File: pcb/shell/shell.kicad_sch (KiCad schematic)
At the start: 206 parts, among them J1 Conn_01x11, J2 Conn_01x11

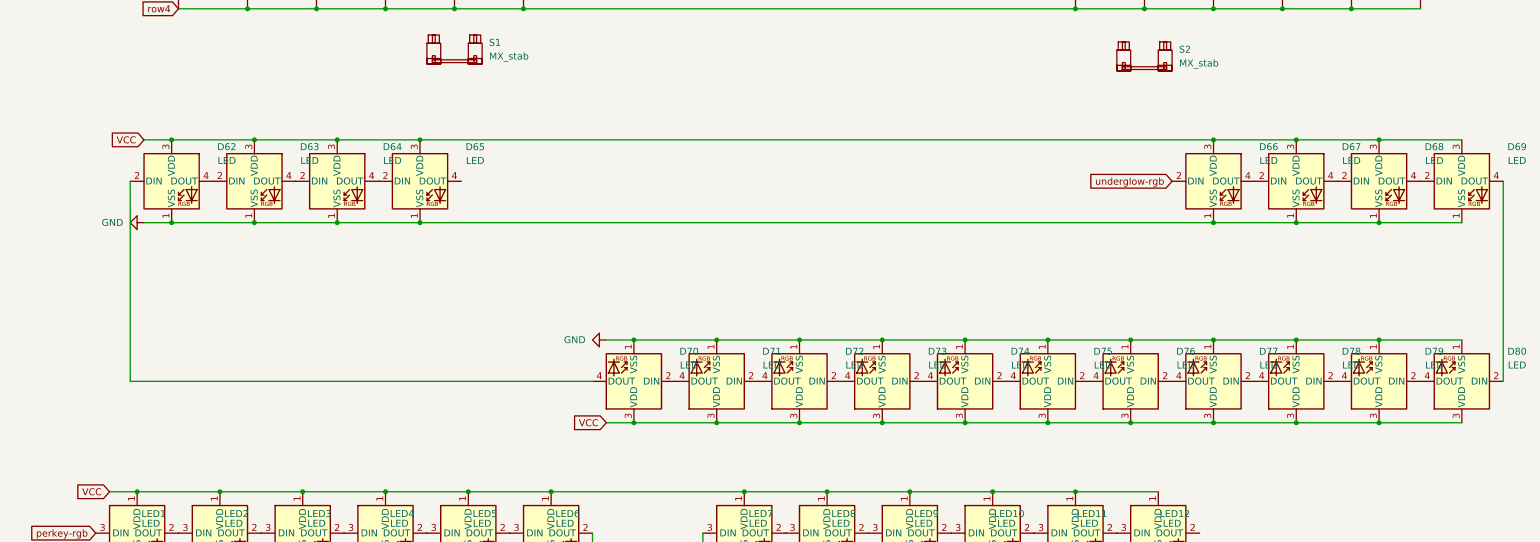
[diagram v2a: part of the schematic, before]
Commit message: added underglow rgb
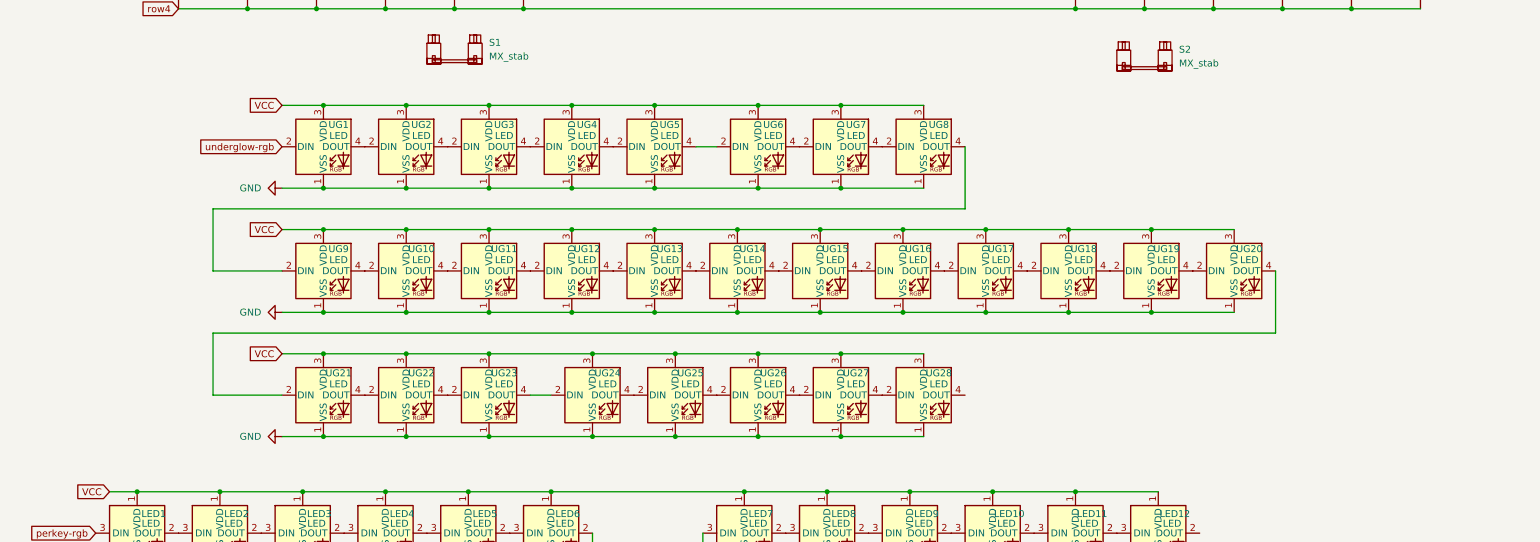
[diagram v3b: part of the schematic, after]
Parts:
- removed D62, D63, D64, D65, D67, D68, D69, D70, D71, D72, D73, D74, D75, D76, D77, D78, D79, D80: LED, LED_SMD:LED_SK6812_PLCC4_5.0x5.0mm_P3.2mm, symbol LED:SK6812
- added UG10, UG11, UG12, UG13, UG14, UG15, UG16, UG17, UG18, UG19, UG2, UG20, UG21, UG22, UG23, UG24, UG25, UG26, UG27, UG28, UG3, UG4, UG5, UG6, UG7, UG8, UG9: LED, LED_SMD:LED_SK6812_PLCC4_5.0x5.0mm_P3.2mm, symbol LED:SK6812
- renumbered D66 to UG1
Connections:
- net GND: now also UG10.1 (VSS), UG11.1 (VSS), UG12.1 (VSS), UG13.1 (VSS), UG14.1 (VSS), UG15.1 (VSS), UG16.1 (VSS), UG17.1 (VSS), UG18.1 (VSS), UG19.1 (VSS), UG2.1 (VSS), UG20.1 (VSS), UG21.1 (VSS), UG22.1 (VSS), UG23.1 (VSS), UG24.1 (VSS), UG25.1 (VSS), UG26.1 (VSS), UG27.1 (VSS), UG28.1 (VSS), UG3.1 (VSS), UG4.1 (VSS), UG5.1 (VSS), UG6.1 (VSS), UG7.1 (VSS), UG8.1 (VSS), UG9.1 (VSS)
- net VCC: now also UG10.3 (VDD), UG11.3 (VDD), UG12.3 (VDD), UG13.3 (VDD), UG14.3 (VDD), UG15.3 (VDD), UG16.3 (VDD), UG17.3 (VDD), UG18.3 (VDD), UG19.3 (VDD), UG2.3 (VDD), UG20.3 (VDD), UG21.3 (VDD), UG22.3 (VDD), UG23.3 (VDD), UG24.3 (VDD), UG25.3 (VDD), UG26.3 (VDD), UG27.3 (VDD), UG28.3 (VDD), UG3.3 (VDD), UG4.3 (VDD), UG5.3 (VDD), UG6.3 (VDD), UG7.3 (VDD), UG8.3 (VDD), UG9.3 (VDD)
- net at UG1.4 (DOUT): now also UG2.2 (DIN)
- new net: UG16.4 (DOUT), UG17.2 (DIN)
- new net: UG17.4 (DOUT), UG18.2 (DIN)
- new net: UG10.4 (DOUT), UG11.2 (DIN)
- new net: UG11.4 (DOUT), UG12.2 (DIN)
- new net: UG13.4 (DOUT), UG14.2 (DIN)
- new net: UG14.4 (DOUT), UG15.2 (DIN)
- new net: UG15.4 (DOUT), UG16.2 (DIN)
- new net: UG26.4 (DOUT), UG27.2 (DIN)
- new net: UG27.4 (DOUT), UG28.2 (DIN)
- new net: UG19.4 (DOUT), UG20.2 (DIN)
- new net: UG20.4 (DOUT), UG21.2 (DIN)
- new net: UG18.4 (DOUT), UG19.2 (DIN)
- new net: UG8.4 (DOUT), UG9.2 (DIN)
- new net: UG10.2 (DIN), UG9.4 (DOUT)
- new net: UG22.4 (DOUT), UG23.2 (DIN)
- new net: UG23.4 (DOUT), UG24.2 (DIN)
- new net: UG21.4 (DOUT), UG22.2 (DIN)
- new net: UG6.4 (DOUT), UG7.2 (DIN)
- new net: UG7.4 (DOUT), UG8.2 (DIN)
- new net: UG24.4 (DOUT), UG25.2 (DIN)
- new net: UG25.4 (DOUT), UG26.2 (DIN)
- new net: UG2.4 (DOUT), UG3.2 (DIN)
- new net: UG3.4 (DOUT), UG4.2 (DIN)
- new net: UG12.4 (DOUT), UG13.2 (DIN)
- new net: UG4.4 (DOUT), UG5.2 (DIN)
- new net: UG5.4 (DOUT), UG6.2 (DIN)
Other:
- moved on the sheet: UG1

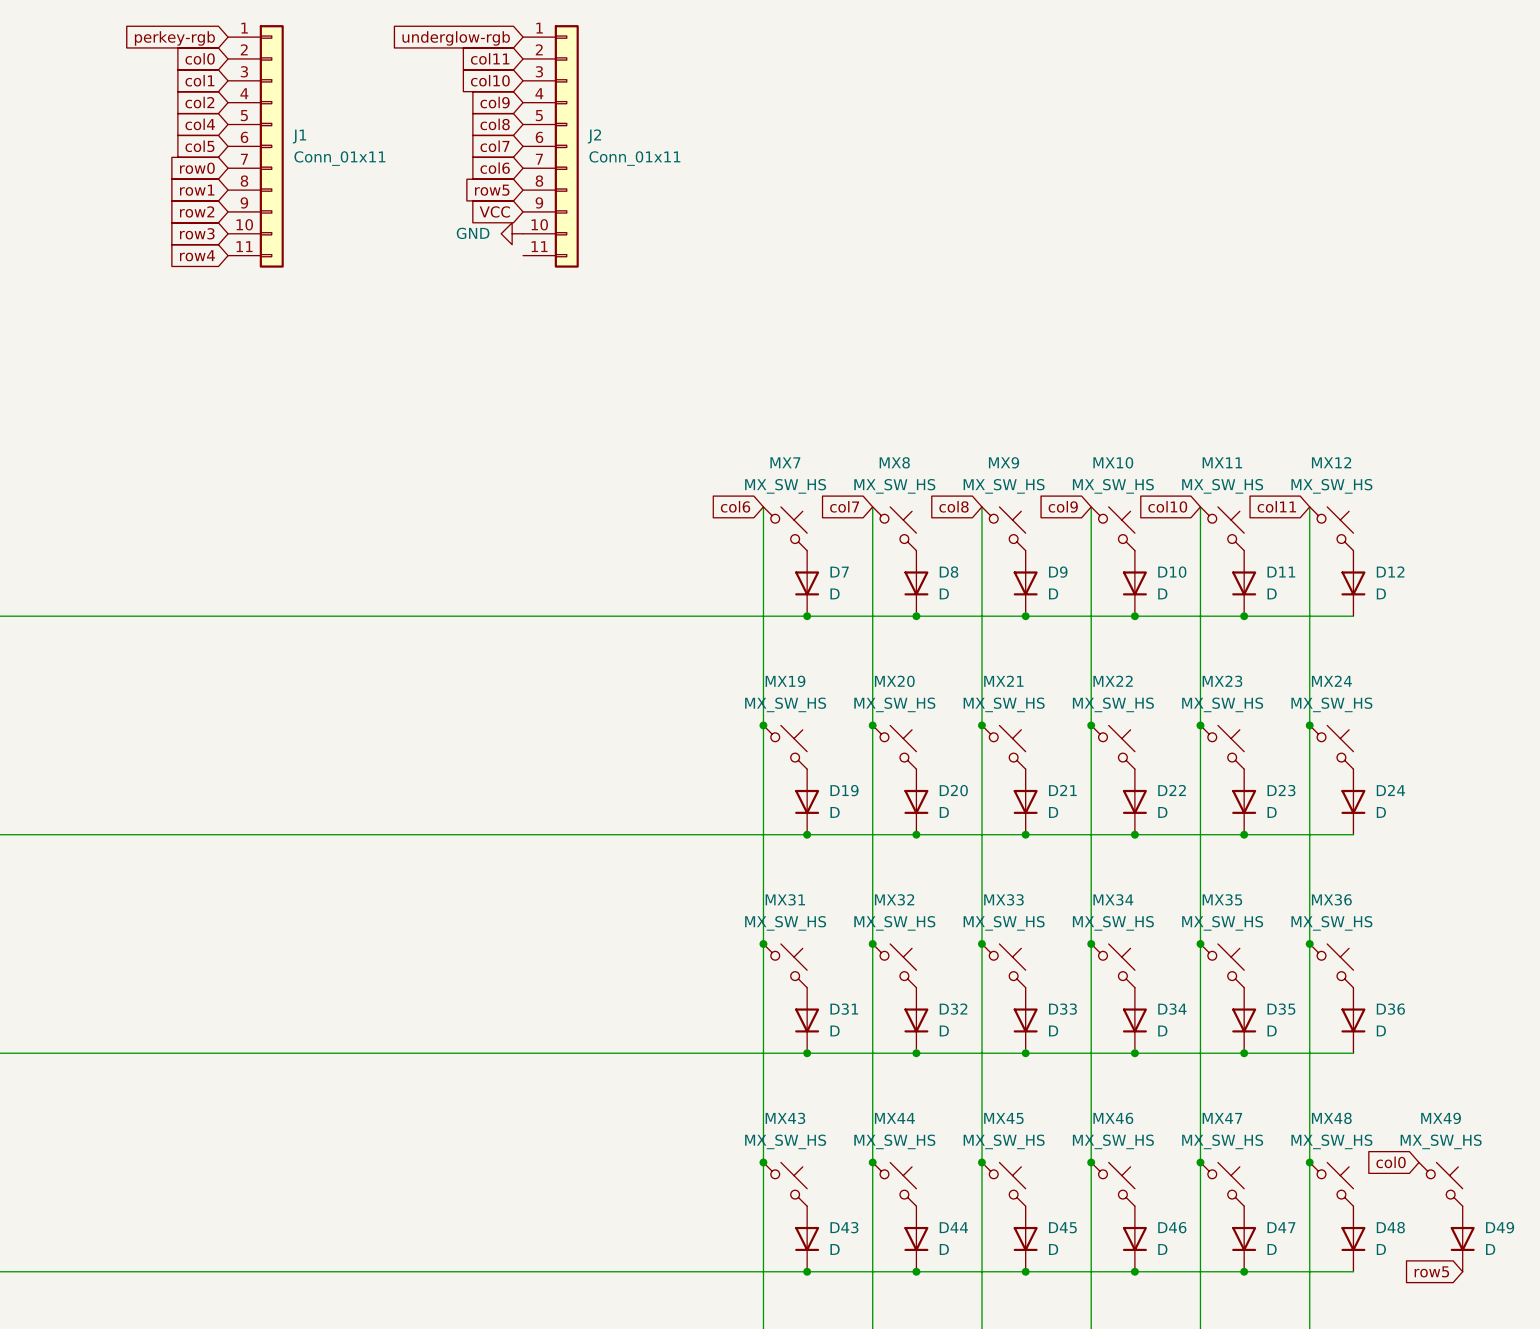
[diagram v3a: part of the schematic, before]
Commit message: last commit before rework without rounded tracks
because of a 100% crash rate when trying to generate the rounded tracks
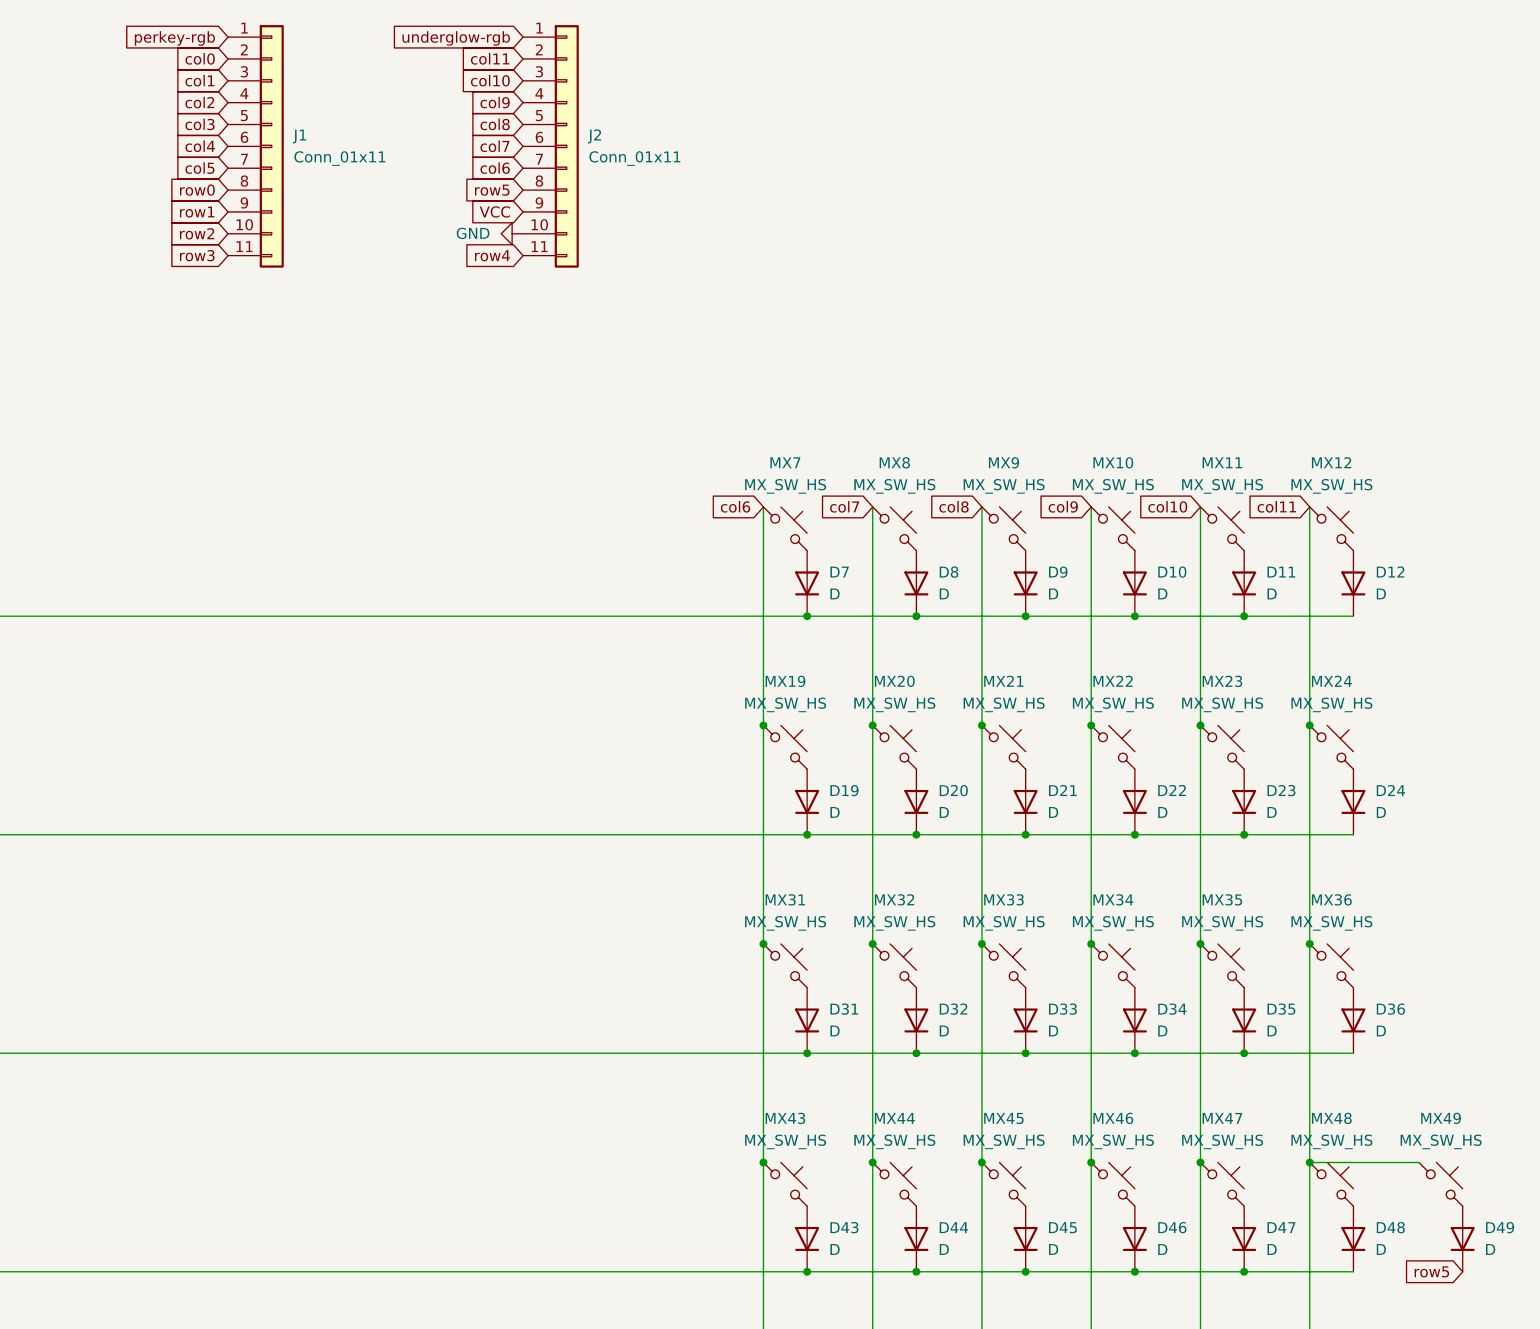
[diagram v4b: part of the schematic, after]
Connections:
- net col0: no longer MX49.1
- net col11: now also MX49.1
- net col3: now also J1.5 (Pin_5)
- net col4: now also J1.6 (Pin_6); no longer J1.5 (Pin_5)
- net col5: now also J1.7 (Pin_7); no longer J1.6 (Pin_6)
- net row0: now also J1.8 (Pin_8); no longer J1.7 (Pin_7)
- net row1: now also J1.9 (Pin_9); no longer J1.8 (Pin_8)
- net row2: now also J1.10 (Pin_10); no longer J1.9 (Pin_9)
- net row3: now also J1.11 (Pin_11); no longer J1.10 (Pin_10)
- net row4: now also J2.11 (Pin_11); no longer J1.11 (Pin_11)

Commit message: finished routing
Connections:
- net col10: now also J2.4 (Pin_4); no longer J2.3 (Pin_3)
- net col11: now also J2.3 (Pin_3); no longer J2.2 (Pin_2)
- net col6: now also J2.8 (Pin_8); no longer J2.7 (Pin_7)
- net col7: now also J2.7 (Pin_7); no longer J2.6 (Pin_6)
- net col8: now also J2.6 (Pin_6); no longer J2.5 (Pin_5)
- net col9: now also J2.5 (Pin_5); no longer J2.4 (Pin_4)
- net row5: now also J2.2 (Pin_2); no longer J2.8 (Pin_8)

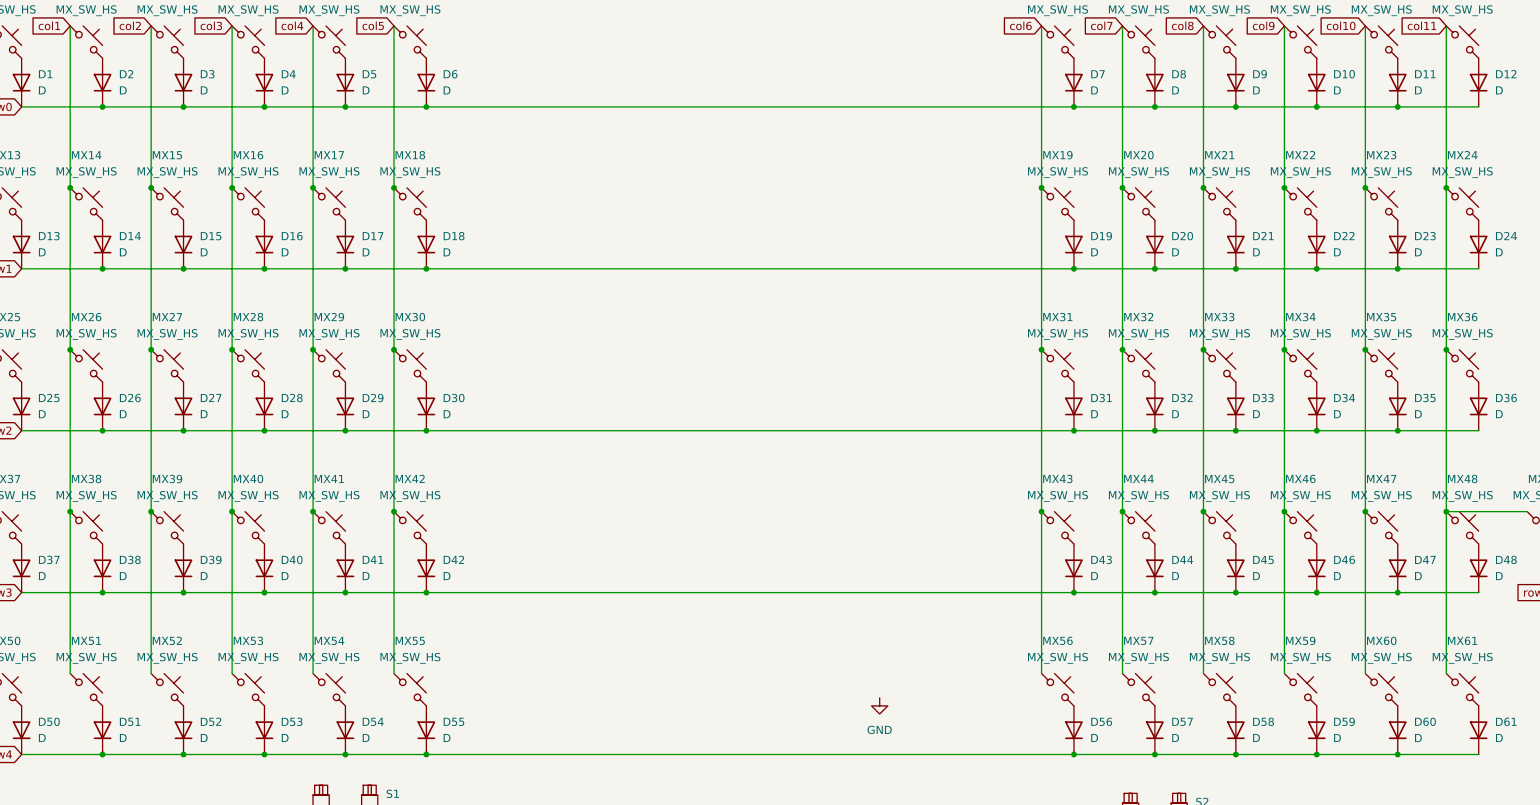
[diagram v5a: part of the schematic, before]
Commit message: added mounting holes
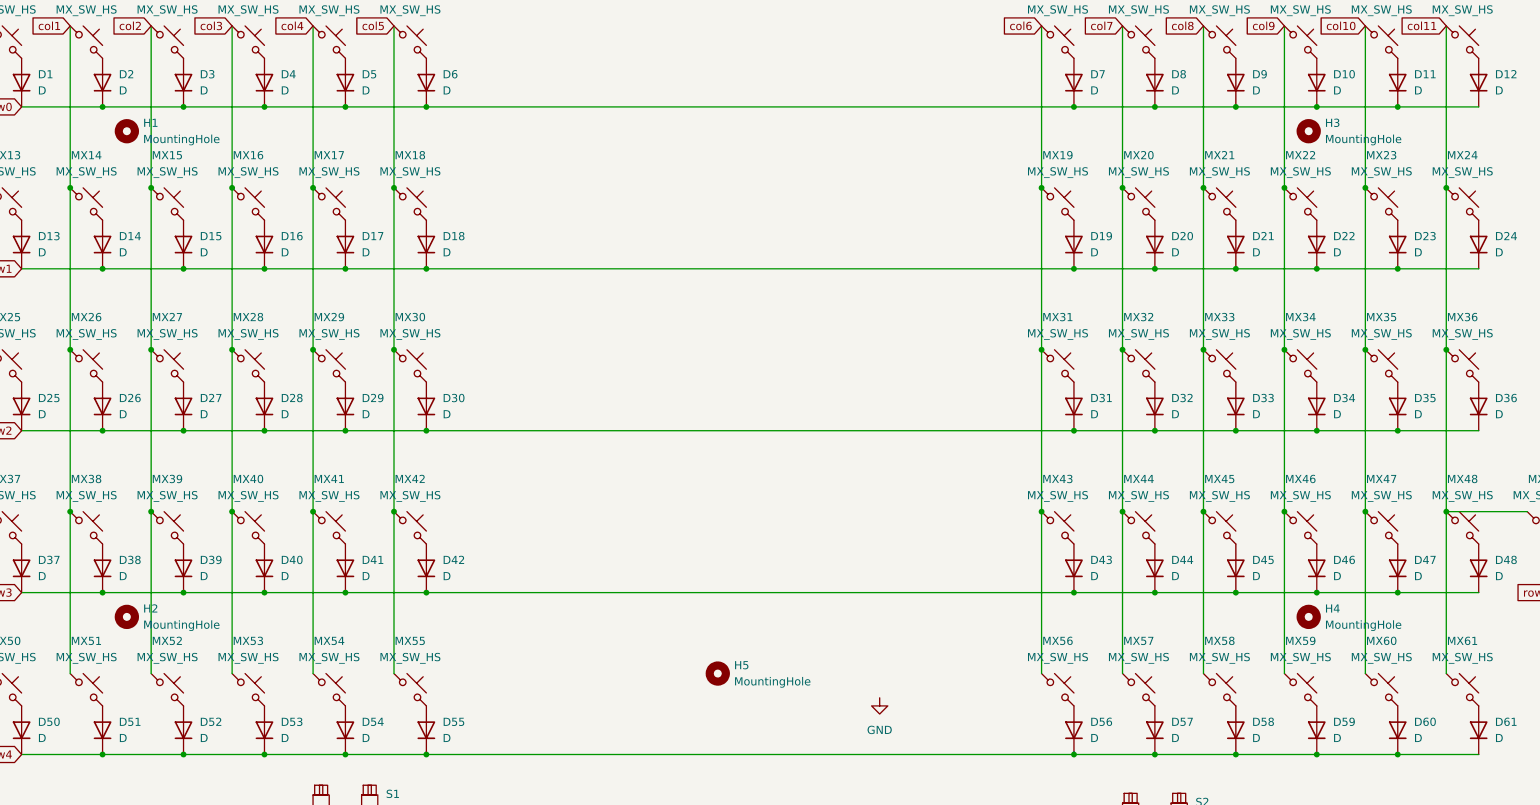
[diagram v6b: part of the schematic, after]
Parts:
- added H1, H2, H3, H4: MountingHole, MountingHole:MountingHole_2.7mm_M2.5_DIN965_Pad, symbol Mechanical:MountingHole
- added H5: MountingHole, MountingHole:MountingHole_3.2mm_M3_DIN965_Pad, symbol Mechanical:MountingHole

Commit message: added core pcb template
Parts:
- J1, J2: footprint Connector_PinSocket_2.54mm:PinSocket_1x11_P2.54mm_Vertical -> Connector_PinHeader_2.54mm:PinHeader_1x11_P2.54mm_Vertical
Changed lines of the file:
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@@
 			)
 		)
-		(property "Footprint" "Connector_PinSocket_2.54mm:PinSocket_1x11_P2.54mm_Vertical"
+		(property "Footprint" "Connector_PinHeader_2.54mm:PinHeader_1x11_P2.54mm_Vertical"
 			(at 167.64 -16.51 0)
 			(effects
@@
 			)
 		)
-		(property "Footprint" "Connector_PinSocket_2.54mm:PinSocket_1x11_P2.54mm_Vertical"
+		(property "Footprint" "Connector_PinHeader_2.54mm:PinHeader_1x11_P2.54mm_Vertical"
 			(at 133.35 -16.51 0)
 			(effects
